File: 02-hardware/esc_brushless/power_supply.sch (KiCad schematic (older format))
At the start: 0 parts

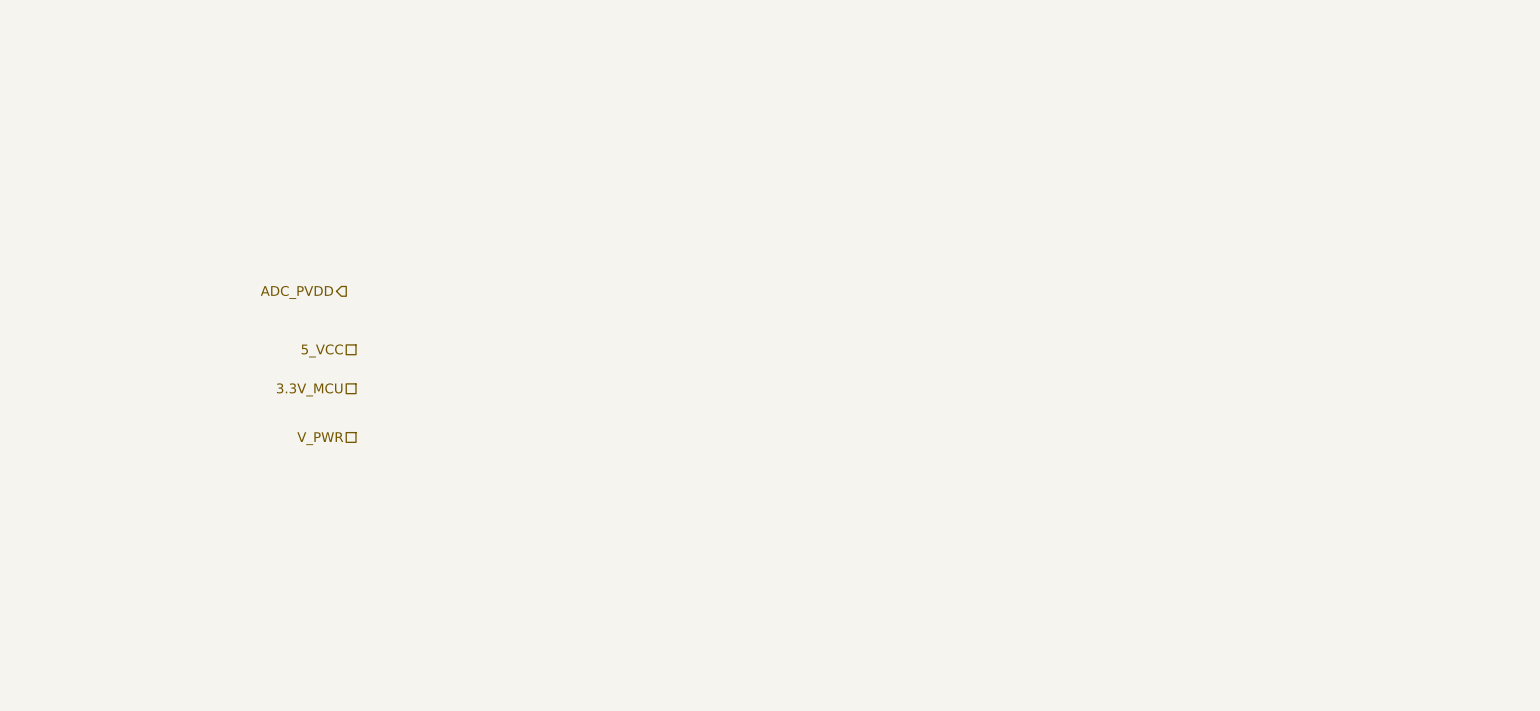
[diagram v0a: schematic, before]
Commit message: Schematics v1.0 - Architecture, microcontroler, global interconnections and IO
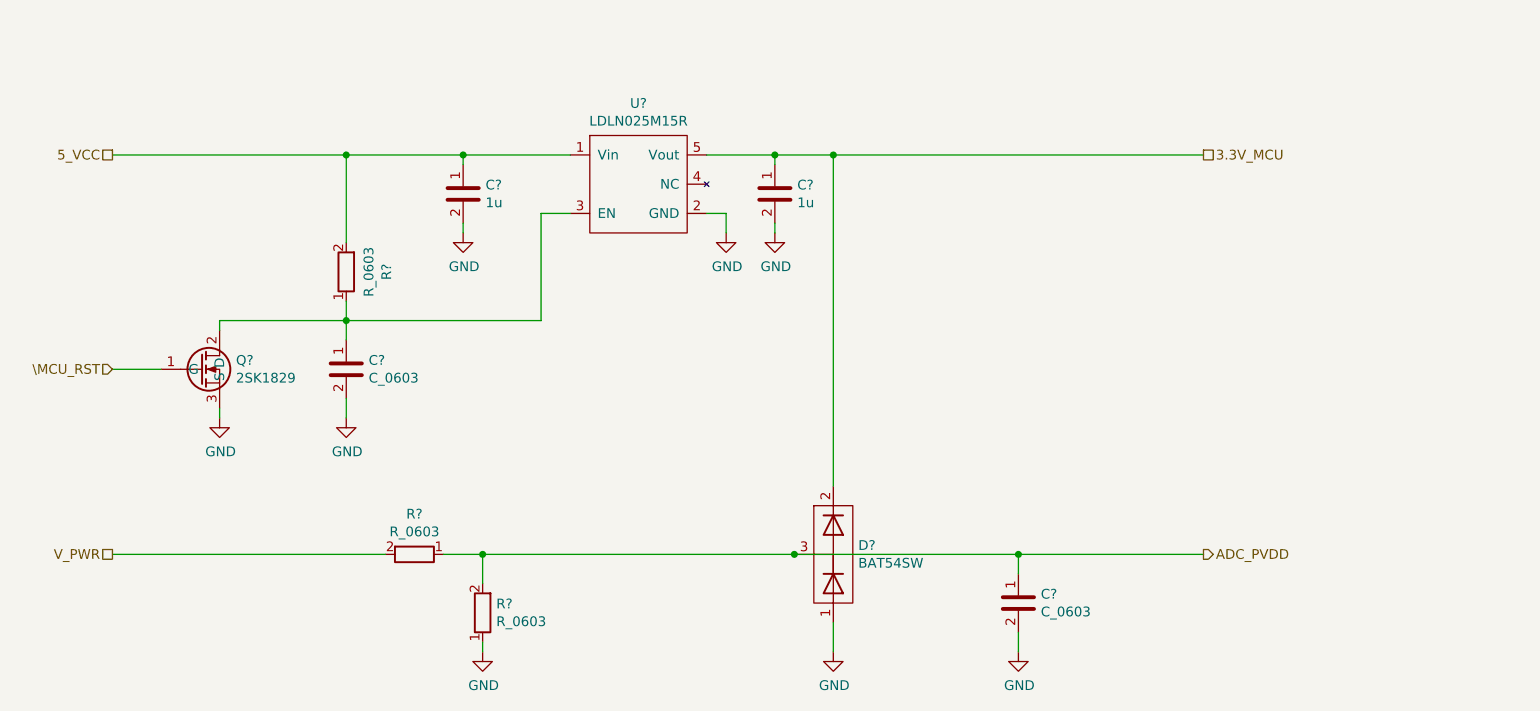
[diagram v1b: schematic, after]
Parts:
- added C? (x2): 1u, p_Package_Capacitor_SMD:C_0603_1608Metric_Pad1.08x0.95mm_HandSolder, symbol p_Passive:C_0603
- added C? (x2): C_0603, p_Package_Capacitor_SMD:C_0603_1608Metric_Pad1.08x0.95mm_HandSolder, symbol p_Passive:C_0603
- added D?: BAT54SW, p_Package_SOT:SOT-323, symbol p_Diode:BAT54SW
- added Q?: 2SK1829, p_Package_SOT:SOT-23, symbol p_Transistor_FET:2SK1829
- added R? (x3): R_0603, p_Package_Resistor_SMD:R_0603_1608Metric_Pad0.98x0.95mm_HandSolder, symbol p_Passive:R_0603
- added U?: LDLN025M15R, p_Package_SOT:SOT-23-5, symbol p_Power_Supply:LDLN025M15R
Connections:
- net 3.3V_MCU: now also C?.1, D?.2 (K), U?.5 (Vout)
- net 5_VCC: now also C?.1, R?.2, U?.1 (Vin)
- net ADC_PVDD: now also C?.1, D?.3 (A/K), R?.1, R?.2
- net V_PWR: now also R?.2
- new net: C?.1, Q?.2 (D), R?.1, U?.3 (EN)
- new net GND: C?.2, C?.2, C?.2, C?.2, D?.1 (A), Q?.3 (S), R?.1, U?.2 (GND)
- new net \MCU_RST: Q?.1 (G)

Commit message: Schematics v1.0 - Architecture, LED, test
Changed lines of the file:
@@
 $Descr A4 11693 8268
 encoding utf-8
-Sheet 5 7
+Sheet 5 6
 Title ""
 Date ""
@@
 Wire Wire Line
 	1750 3700 2000 3700
+Text HLabel 7350 5050 2    50   UnSpc ~ 0
+GND
+$Comp
+L power:GND #PWR?
+U 1 1 60BED520
+P 7250 5150
+F 0 "#PWR?" H 7250 4900 50  0001 C CNN
+F 1 "GND" H 7255 4977 50  0000 C CNN
+F 2 "" H 7250 5150 50  0001 C CNN
+F 3 "" H 7250 5150 50  0001 C CNN
+	1    7250 5150
+	1    0    0    -1
+$EndComp
+Wire Wire Line
+	7350 5050 7250 5050
+Wire Wire Line
+	7250 5050 7250 5150
 $EndSCHEMATC

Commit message: Schematics v1.0 - Fix DRC issues
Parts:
- gave numbers to parts that had none: 10
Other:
- moved on the sheet: C30, C31, C32, C33, D3, Q8, R42, R43, R44, U3
